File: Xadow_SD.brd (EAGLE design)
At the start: 25.5 x 20.4 mm, 7 parts, among them IC1 4050D, J1 MICRO-SDCARD-CONNECTOR-330006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, J2 12p FPC bottom contact, J3 12p FPC bottom contact, J4 CONNECTOR-HEADER-6P-3460650P1

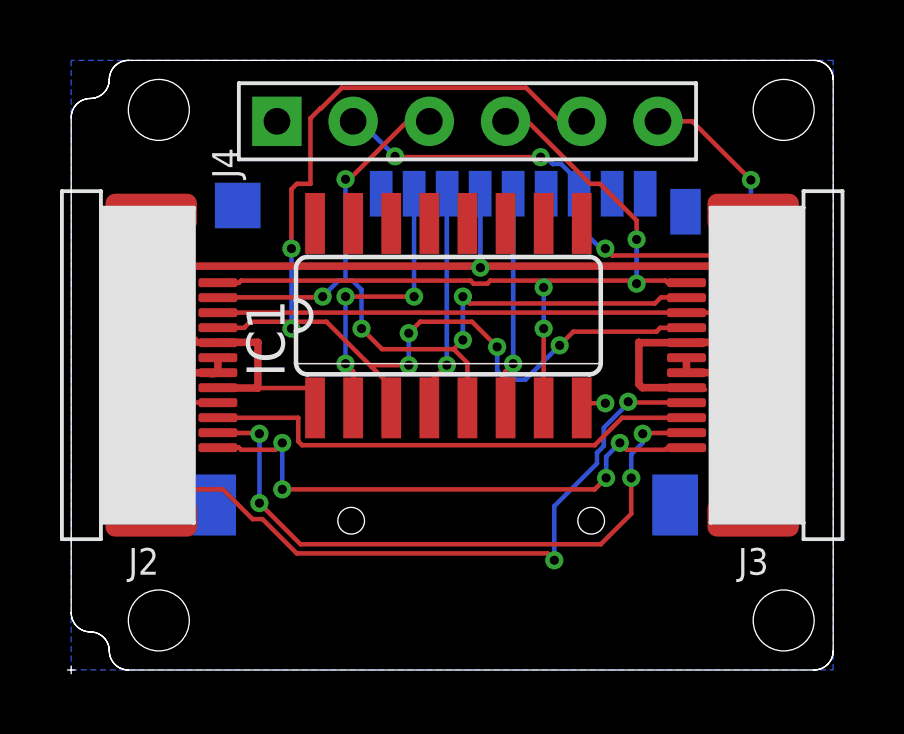
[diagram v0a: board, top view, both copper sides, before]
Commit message: Neaten up routing
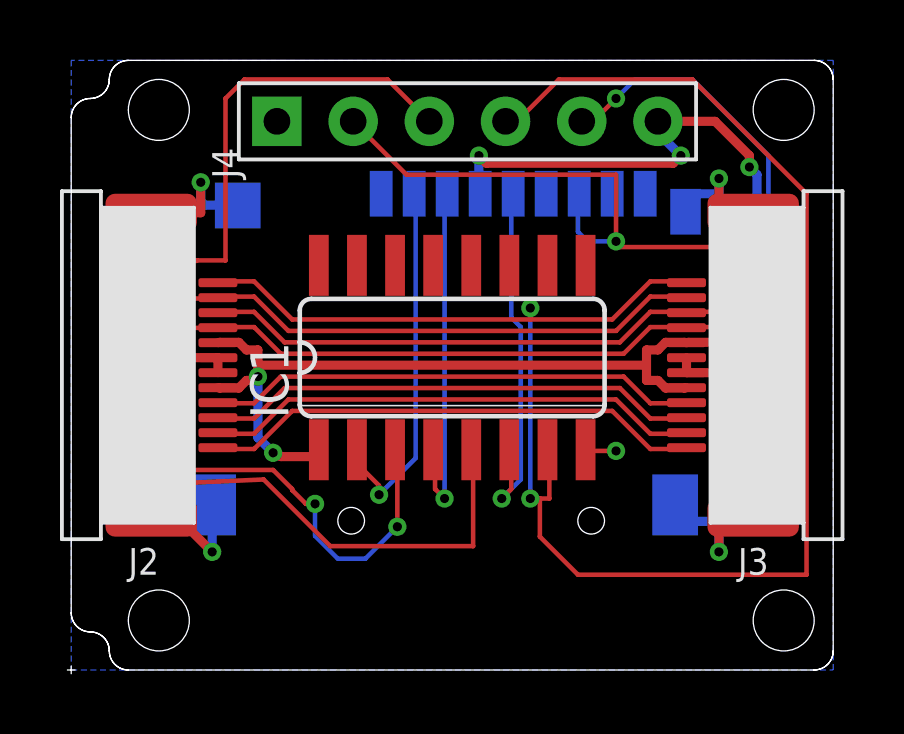
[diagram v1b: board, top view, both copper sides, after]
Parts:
- moved IC1 1.40 mm to (20.6, 16.8)
- moved U$2 0.76 mm to (31.1, 11.9)
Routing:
- net PB1/D15/SCK: track 28.0 -> 61.3 mm, vias 4 -> 2
- net PB2/D16/MOSI: track 28.4 -> 58.9 mm, vias 5 -> 0
- net PF0/A5: track 38.9 -> 54.1 mm, vias 6 -> 4
- net PD0/SCL/D3: track 26.0 -> 16.4 mm, vias 4 -> 0
- net PB3/D14/MISO: track 34.1 -> 41.3 mm, vias 5 -> 1
- net SCK: track 7.24 -> 12.4 mm
- net PD2/RXI/D0: track 21.4 -> 16.6 mm, vias 4 -> 0
- net MOSI: track 7.39 -> 12.0 mm
- net GND: track 33.2 -> 29.9 mm, vias 3 -> 6
- net CS: track 9.53 -> 12.4 mm, vias 3 -> 1
- net PD3/TXO/D1: track 18.5 -> 16.7 mm, vias 4 -> 0
- net 3V3: track 49.2 -> 47.4 mm, vias 3 -> 6

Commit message: Flip SD holder
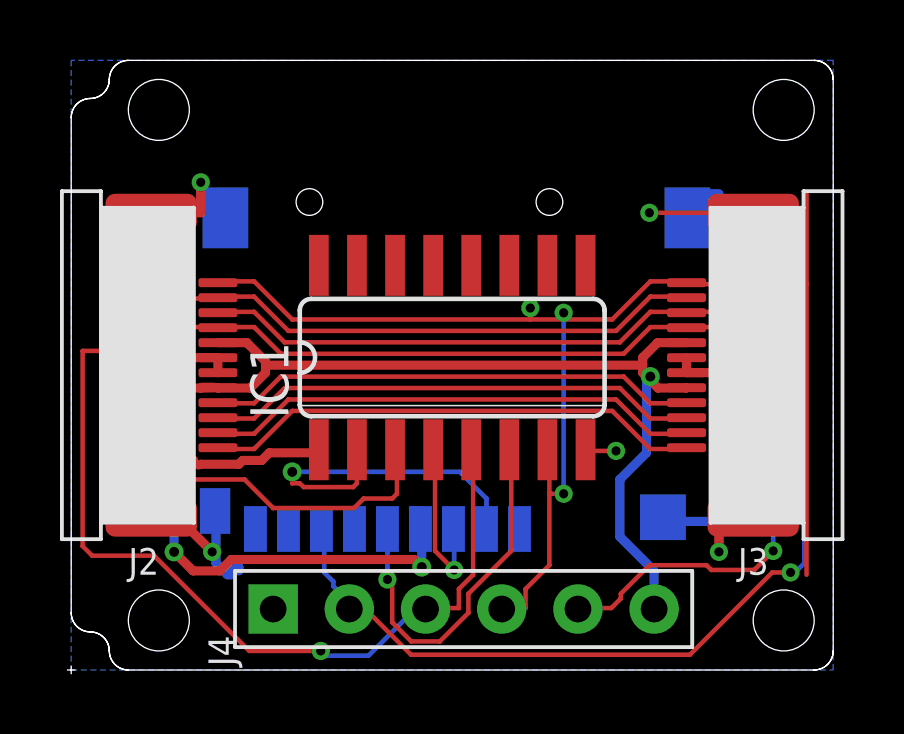
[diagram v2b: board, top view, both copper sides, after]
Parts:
- removed U$2: (no value), Logo:LOGO_SILK
- moved J4 16.3 mm to (21.0, 8.38)
- moved J1 3.83 mm to (20.7, 18.5), turned to 90 degrees
- moved U$3 3.70 mm to (32.6, 19.2)
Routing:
- net PB1/D15/SCK: track 61.3 -> 47.0 mm, vias 2 -> 3
- net PB2/D16/MOSI: track 58.9 -> 48.6 mm, vias 0 -> 1
- net PB3/D14/MISO: track 41.3 -> 48.4 mm, vias 1 -> 2
- net MOSI: track 12.0 -> 5.67 mm
- net 3V3: track 47.4 -> 53.3 mm, vias 6 -> 4
- net GND: track 29.9 -> 31.7 mm
- net PF0/A5: track 54.1 -> 52.5 mm, vias 4 -> 2
- net CS: track 12.4 -> 11.6 mm

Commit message: Change VCC wire width
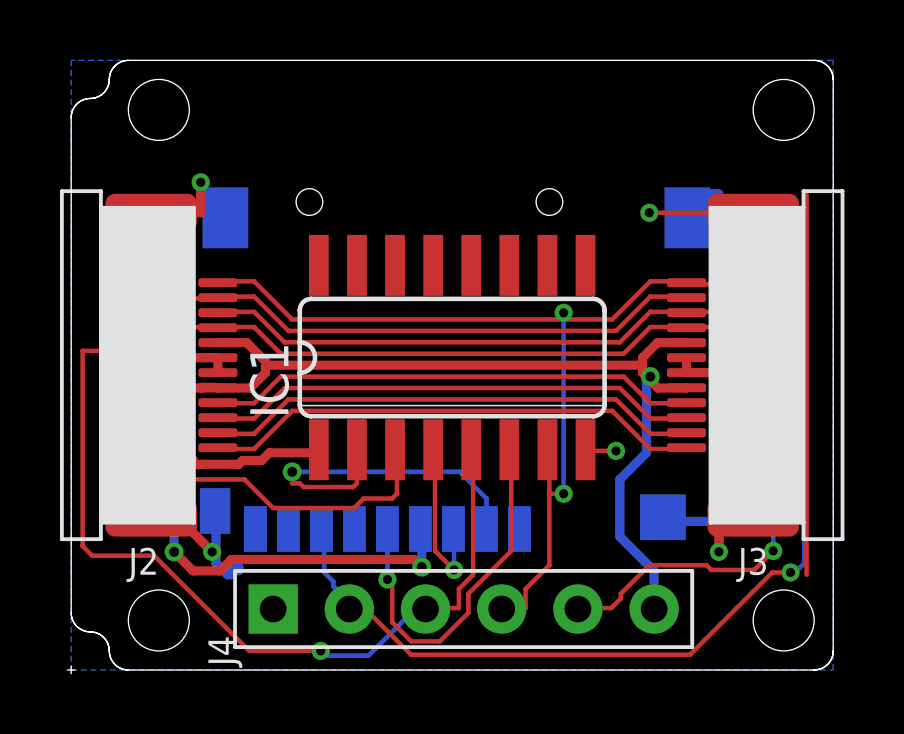
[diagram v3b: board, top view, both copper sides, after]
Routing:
- net PB1/D15/SCK: track 47.0 -> 46.6 mm, vias 3 -> 2
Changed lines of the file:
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@@
 <wire x1="27.178" y1="19.304" x2="28.321" y2="19.304" width="0.1524" layer="1"/>
 <wire x1="25.908" y1="18.034" x2="27.178" y2="19.304" width="0.1524" layer="1"/>
-<wire x1="15.24" y1="18.034" x2="23.1775" y2="18.034" width="0.1524" layer="1"/>
-<wire x1="23.1775" y1="18.034" x2="24.28875" y2="18.034" width="0.1524" layer="1"/>
+<wire x1="15.24" y1="18.034" x2="24.28875" y2="18.034" width="0.1524" layer="1"/>
 <wire x1="24.28875" y1="18.034" x2="25.908" y2="18.034" width="0.1524" layer="1"/>
 <wire x1="13.97" y1="19.304" x2="15.24" y2="18.034" width="0.1524" layer="1"/>
@@
 <wire x1="28.321" y1="19.304" x2="28.384" y2="19.26" width="0.1524" layer="1"/>
 <wire x1="12.827" y1="19.304" x2="12.764" y2="19.26" width="0.1524" layer="1"/>
-<wire x1="23.1775" y1="18.034" x2="23.1775" y2="18.415" width="0.1524" layer="1"/>
-<via x="23.1775" y="18.415" extent="1-16" drill="0.3048"/>
 <wire x1="32.385" y1="9.525" x2="32.385" y2="19.20875" width="0.1524" layer="1"/>
 <wire x1="32.385" y1="19.20875" x2="32.385" y2="22.225" width="0.1524" layer="1"/>
